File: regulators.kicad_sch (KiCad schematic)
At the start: 99 parts, among them IC1 IAUCN04S7L028ATMA1, Q6 Si7149DP, Q7 CSD17577Q3A, Q8 CSD17313Q2, Q9 CSD17578Q3A, U19 TPS611781RNWR, U20 XLM51772RHAR, U3 AP64501SP-13, U6 AP64501SP-13, U7 AP64501SP-13

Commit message: standardised components
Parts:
- R59: LCSC C138687 -> C4180598
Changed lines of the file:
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@@
 			)
 		)
-		(property "LCSC" "C138687"
+		(property "LCSC" "C4180598"
 			(at 269.24 64.77 0)
 			(effects

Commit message: standardised components, removing mixed values
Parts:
- C107, C109, C110, C86: LCSC C1525 -> C307331
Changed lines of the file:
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@@
 			)
 		)
-		(property "LCSC" "C1525"
+		(property "LCSC" "C307331"
 			(at 205.74 245.11 0)
 			(effects
@@
 			)
 		)
-		(property "LCSC" "C1525"
+		(property "LCSC" "C307331"
 			(at 43.18 245.11 0)
 			(effects
@@
 			)
 		)
-		(property "LCSC" "C1525"
+		(property "LCSC" "C307331"
 			(at 193.04 242.57 0)
 			(effects
@@
 			)
 		)
-		(property "LCSC" "C1525"
+		(property "LCSC" "C307331"
 			(at 257.81 50.8 0)
 			(effects

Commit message: ALL LCSC PARTS DONE
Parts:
- Q6: LCSC (none) -> C553982
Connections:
- net +19V: now also Q6.5 (D); no longer Q6.1 (S), Q6.2 (S), Q6.3 (S)
- net 19V_VOUT: now also Q6.1 (S), Q6.2 (S), Q6.3 (S); no longer Q6.5 (D)
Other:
- moved on the sheet: Q6
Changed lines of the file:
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@@
 	(symbol
 		(lib_id "Transistor_FET:Si7141DP")
-		(at 294.64 62.23 90)
+		(at 294.64 62.23 270)
+		(mirror x)
 		(unit 1)
 		(exclude_from_sim no)
@@
 		(on_board yes)
 		(dnp no)
-		(fields_autoplaced yes)
 		(property "Reference" "Q6"
 			(at 294.64 53.34 90)
@@
 		)
 		(property "Footprint" "Package_SO:PowerPAK_SO-8_Single"
-			(at 296.545 57.15 0)
+			(at 292.735 57.15 0)
 			(effects
 				(font
@@
 		)
 		(property "Datasheet" "https://www.vishay.com/docs/65596/si7141dp.pdf"
-			(at 298.45 57.15 0)
+			(at 290.83 57.15 0)
 			(effects
 				(font
@@
 			)
 		)
-		(property "LCSC" ""
+		(property "LCSC" "C553982"
 			(at 294.64 62.23 90)
 			(effects

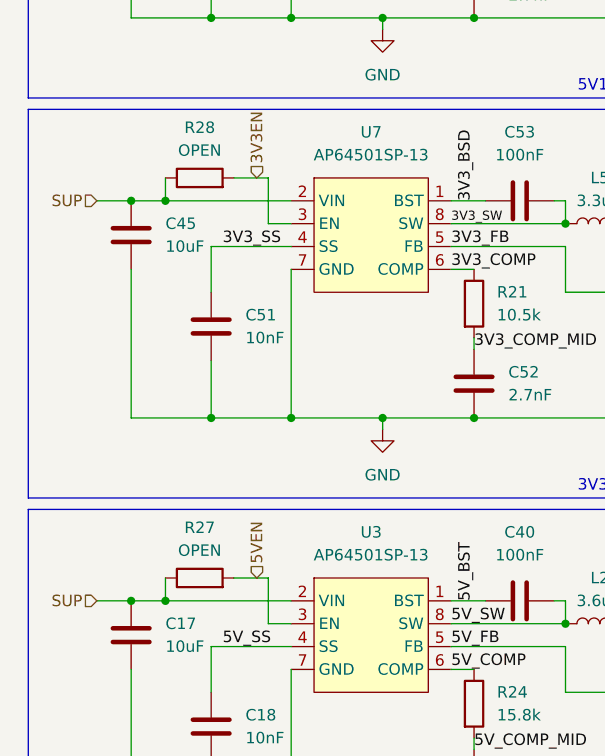
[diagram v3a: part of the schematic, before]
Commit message: Fixed errors with open resistors and led
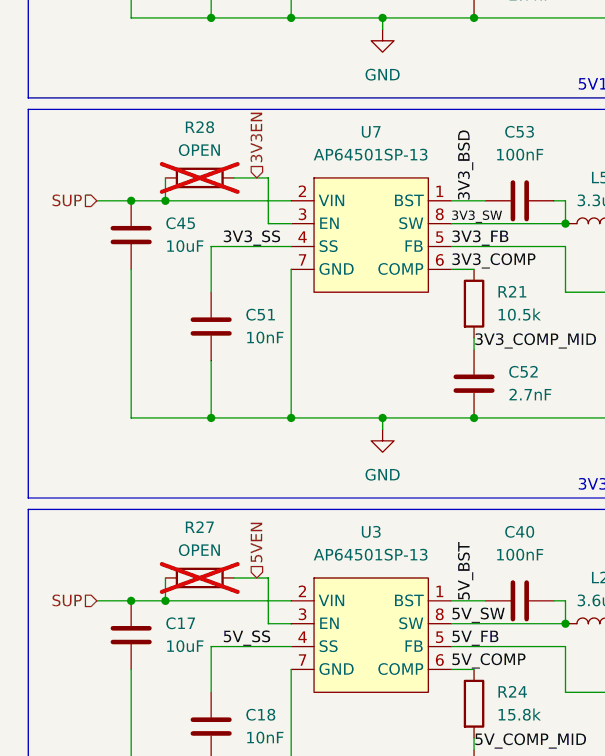
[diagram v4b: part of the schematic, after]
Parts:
- R27, R28: now not fitted; now left out of the parts list
- R69, R71: LCSC C6779318 -> C851068
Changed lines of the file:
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@@
 		(unit 1)
 		(exclude_from_sim no)
-		(in_bom yes)
+		(in_bom no)
 		(on_board yes)
-		(dnp no)
+		(dnp yes)
 		(property "Reference" "R27"
 			(at 39.37 107.442 90)
@@
 			)
 		)
-		(property "LCSC" "C6779318"
+		(property "LCSC" "C851068"
 			(at 210.82 196.85 0)
 			(effects
@@
 			)
 		)
-		(property "LCSC" "C6779318"
+		(property "LCSC" "C851068"
 			(at 312.42 185.42 0)
 			(effects
@@
 		(unit 1)
 		(exclude_from_sim no)
-		(in_bom yes)
+		(in_bom no)
 		(on_board yes)
-		(dnp no)
+		(dnp yes)
 		(property "Reference" "R28"
 			(at 39.37 62.992 90)

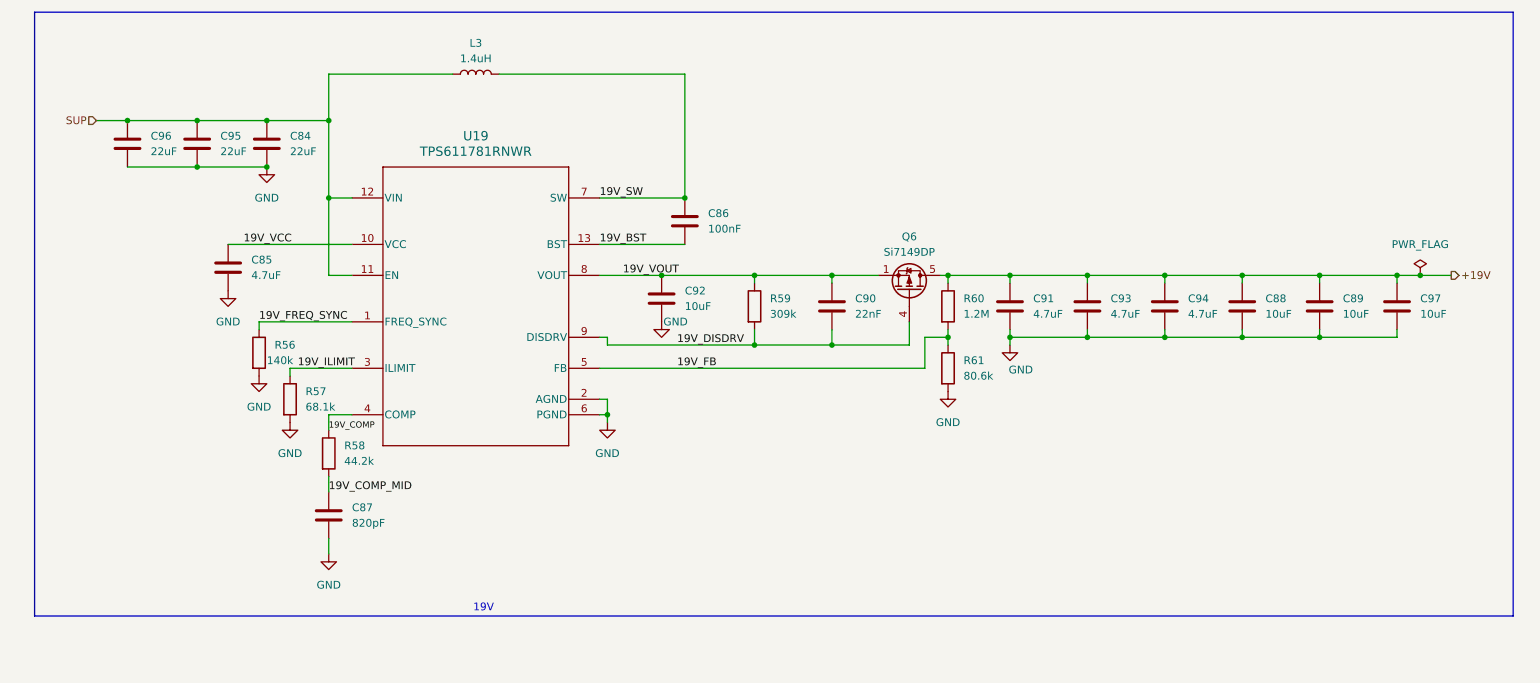
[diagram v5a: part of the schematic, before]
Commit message: Marked 19V regulator as DNP to simplify next board iteration
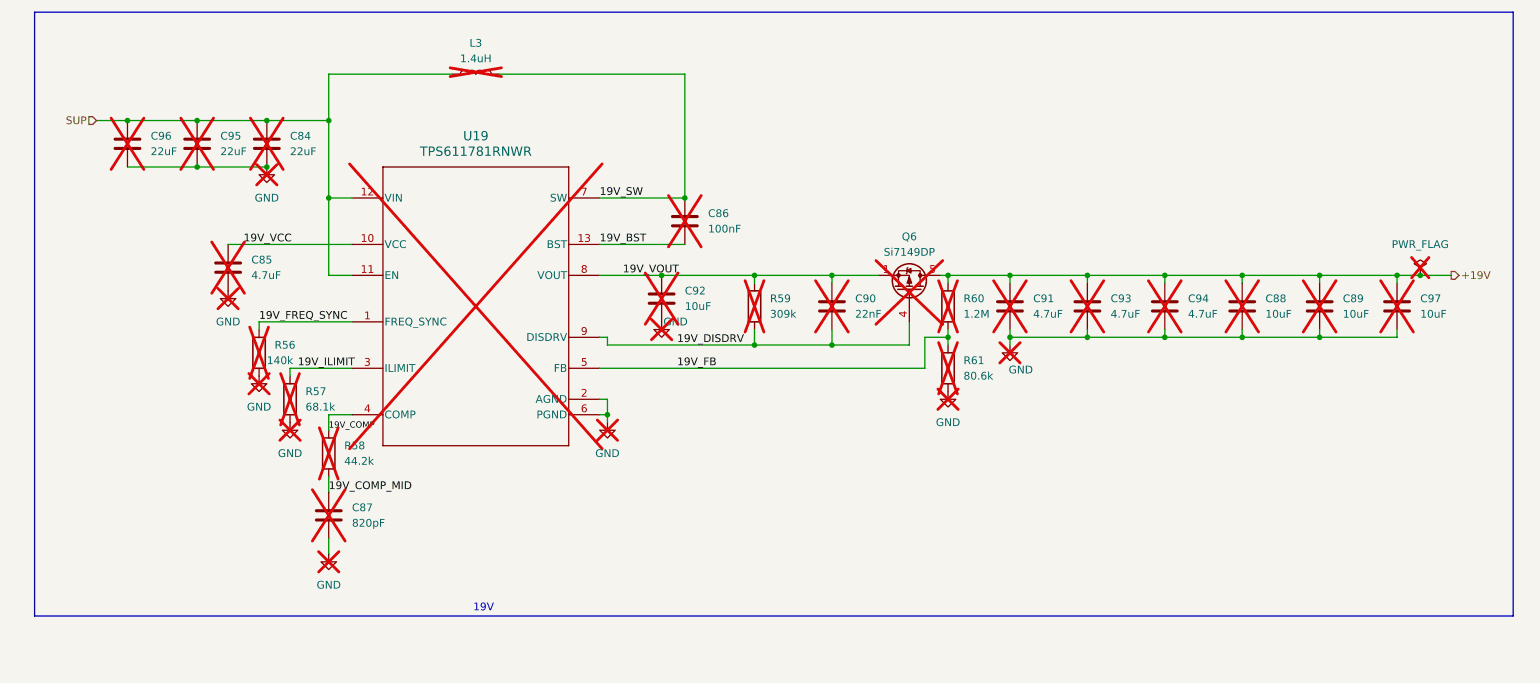
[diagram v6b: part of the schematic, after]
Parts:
- C84, C85, C86, C87, C88, C89, C90, C91, C92, C93, C94, C95, C96, C97, L3, Q6, R56, R57, R58, R59, R60, R61, U19: now not fitted
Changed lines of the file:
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@@
 		(on_board yes)
 		(in_pos_files yes)
-		(dnp no)
+		(dnp yes)
 		(fields_autoplaced yes)
 		(property "Reference" "#PWR0125"
@@
 		(on_board yes)
 		(in_pos_files yes)
-		(dnp no)
+		(dnp yes)
 		(property "Reference" "#PWR0133"
 			(at 311.15 77.47 0)
@@
 		(on_board yes)
 		(in_pos_files yes)
-		(dnp no)
+		(dnp yes)
 		(fields_autoplaced yes)
 		(property "Reference" "R60"
@@
 		(on_board yes)
 		(in_pos_files yes)
-		(dnp no)
+		(dnp yes)
 		(fields_autoplaced yes)
 		(property "Reference" "C85"
@@
 		(on_board yes)
 		(in_pos_files yes)
-		(dnp no)
+		(dnp yes)
 		(fields_autoplaced yes)
 		(property "Reference" "#PWR0130"
@@
 		(on_board yes)
 		(in_pos_files yes)
-		(dnp no)
+		(dnp yes)
 		(fields_autoplaced yes)
 		(property "Reference" "L3"
@@
 		(on_board yes)
 		(in_pos_files yes)
-		(dnp no)
+		(dnp yes)
 		(fields_autoplaced yes)
 		(property "Reference" "C95"
@@
 		(on_board yes)
 		(in_pos_files yes)
-		(dnp no)
+		(dnp yes)
 		(fields_autoplaced yes)
 		(property "Reference" "#PWR0132"
@@
 		(on_board yes)
 		(in_pos_files yes)
-		(dnp no)
+		(dnp yes)
 		(fields_autoplaced yes)
 		(property "Reference" "C90"
@@
 		(on_board yes)
 		(in_pos_files yes)
-		(dnp no)
+		(dnp yes)
 		(fields_autoplaced yes)
 		(property "Reference" "U19"
@@
 		(on_board yes)
 		(in_pos_files yes)
-		(dnp no)
+		(dnp yes)
 		(property "Reference" "C92"
 			(at 257.81 62.2299 0)
@@
 		(on_board yes)
 		(in_pos_files yes)
-		(dnp no)
+		(dnp yes)
 		(fields_autoplaced yes)
 		(property "Reference" "#PWR0127"
@@
 		(on_board yes)
 		(in_pos_files yes)
-		(dnp no)
+		(dnp yes)
 		(fields_autoplaced yes)
 		(property "Reference" "C88"
@@
 		(on_board yes)
 		(in_pos_files yes)
-		(dnp no)
+		(dnp yes)
 		(fields_autoplaced yes)
 		(property "Reference" "C96"
@@
 		(on_board yes)
 		(in_pos_files yes)
-		(dnp no)
+		(dnp yes)
 		(fields_autoplaced yes)
 		(property "Reference" "C87"
@@
 		(on_board yes)
 		(in_pos_files yes)
-		(dnp no)
+		(dnp yes)
 		(fields_autoplaced yes)
 		(property "Reference" "R57"
@@
 		(on_board yes)
 		(in_pos_files yes)
-		(dnp no)
+		(dnp yes)
 		(fields_autoplaced yes)
 		(property "Reference" "#FLG06"
@@
 		(on_board yes)
 		(in_pos_files yes)
-		(dnp no)
+		(dnp yes)
 		(fields_autoplaced yes)
 		(property "Reference" "#PWR0128"
@@
 		(on_board yes)
 		(in_pos_files yes)
-		(dnp no)
+		(dnp yes)
 		(fields_autoplaced yes)
 		(property "Reference" "C91"
@@
 		(on_board yes)
 		(in_pos_files yes)
-		(dnp no)
+		(dnp yes)
 		(property "Reference" "Q6"
 			(at 294.64 53.34 90)
@@
 		(on_board yes)
 		(in_pos_files yes)
-		(dnp no)
+		(dnp yes)
 		(fields_autoplaced yes)
 		(property "Reference" "C89"
@@
 		(on_board yes)
 		(in_pos_files yes)
-		(dnp no)
+		(dnp yes)
 		(fields_autoplaced yes)
 		(property "Reference" "C97"
@@
 		(on_board yes)
 		(in_pos_files yes)
-		(dnp no)
+		(dnp yes)
 		(property "Reference" "R56"
 			(at 190.5 71.1199 0)
@@
 		(on_board yes)
 		(in_pos_files yes)
-		(dnp no)
+		(dnp yes)
 		(fields_autoplaced yes)
 		(property "Reference" "R59"
@@
 		(on_board yes)
 		(in_pos_files yes)
-		(dnp no)
+		(dnp yes)
 		(fields_autoplaced yes)
 		(property "Reference" "R61"
@@
 		(on_board yes)
 		(in_pos_files yes)
-		(dnp no)
+		(dnp yes)
 		(fields_autoplaced yes)
 		(property "Reference" "C93"
@@
 		(on_board yes)
 		(in_pos_files yes)
-		(dnp no)
+		(dnp yes)
 		(fields_autoplaced yes)
 		(property "Reference" "#PWR0126"
@@
 		(on_board yes)
 		(in_pos_files yes)
-		(dnp no)
+		(dnp yes)
 		(fields_autoplaced yes)
 		(property "Reference" "C86"
@@
 		(on_board yes)
 		(in_pos_files yes)
-		(dnp no)
+		(dnp yes)
 		(fields_autoplaced yes)
 		(property "Reference" "#PWR0129"
@@
 		(on_board yes)
 		(in_pos_files yes)
-		(dnp no)
+		(dnp yes)
 		(fields_autoplaced yes)
 		(property "Reference" "C84"
@@
 		(on_board yes)
 		(in_pos_files yes)
-		(dnp no)
+		(dnp yes)
 		(fields_autoplaced yes)
 		(property "Reference" "C94"
@@
 		(on_board yes)
 		(in_pos_files yes)
-		(dnp no)
+		(dnp yes)
 		(fields_autoplaced yes)
 		(property "Reference" "R58"
@@
 		(on_board yes)
 		(in_pos_files yes)
-		(dnp no)
+		(dnp yes)
 		(property "Reference" "#PWR0134"
 			(at 254 73.66 0)

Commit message: does this work
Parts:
- R67: LCSC C2479048 -> C92124
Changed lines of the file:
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@@
 			)
 		)
-		(property "LCSC" "C2479048"
+		(property "LCSC" "C92124"
 			(at 247.65 190.5 90)
 			(hide yes)
